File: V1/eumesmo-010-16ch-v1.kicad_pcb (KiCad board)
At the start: 4 copper layers, 128 x 67.8 mm, 284 parts, among them J1 250-208, J2 250-208, J3 250-208, J4 250-208, J5 250-202, J6 USB_C_Receptacle_USB2.0, J7 ETHERNET, Q1 WPM2015-3/TR, Q2 MMUN2211LT3G, Q3 UMH3N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

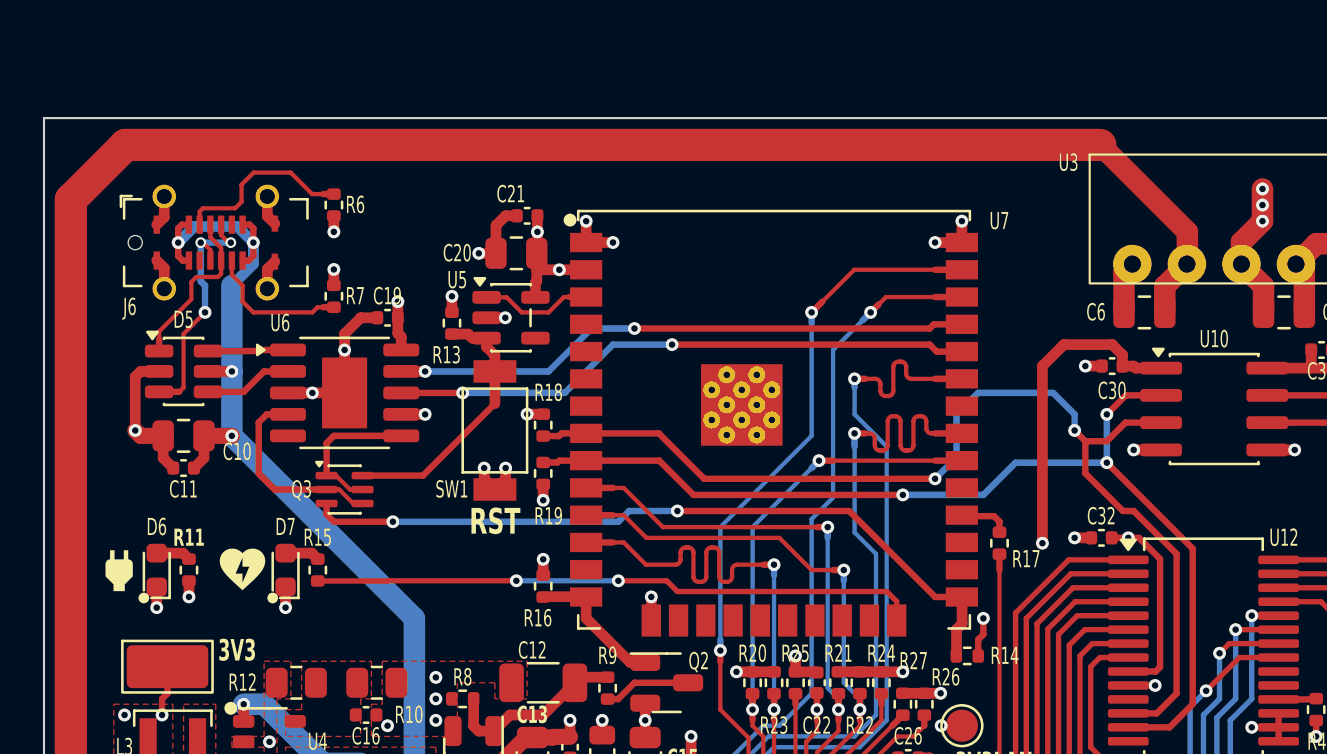
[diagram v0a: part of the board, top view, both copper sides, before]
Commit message: Power and heartbeat leds repositioned.
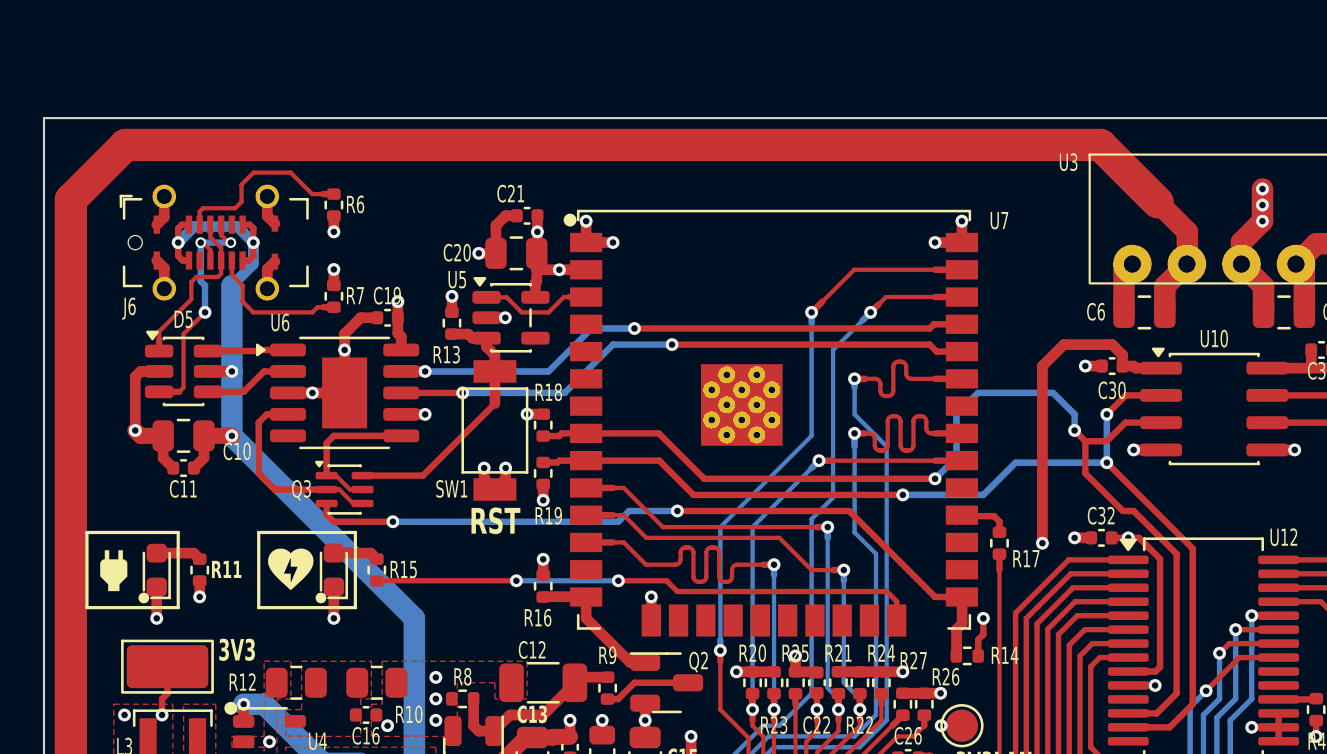
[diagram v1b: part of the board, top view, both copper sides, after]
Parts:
- moved R15 2.75 mm to (105.3, 87.3)
- moved D7 2.25 mm to (103.3, 87.3)
- moved REF** 2.25 mm to (101.3, 87.3)
- moved R11 0.50 mm to (97.0, 87.3)
- moved REF** 0.25 mm to (93.0, 87.3)
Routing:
- net /MCU/CPUOK: track 28.3 -> 25.5 mm
- net GND: track 72.2 -> 73.2 mm
- net /Power/3V3LED: track 1.61 -> 2.11 mm
- net /MCU/CPULED: track 1.61 -> 2.11 mm
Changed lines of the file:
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@@
 	(footprint "Tales:R_0402_1005Metric"
 		(layer "F.Cu")
-		(at 102.52 87.33 90)
+		(at 105.27 87.33 90)
 		(descr "Resistor SMD 0402 (1005 Metric), square (rectangular) end terminal, IPC_7351 nominal, (Body size source: IPC-SM-782 page 72, https://www.pcb-3d.com/wordpress/wp-content/uploads/ipc-sm-782a_amendment_1_and_2.pdf), generated with kicad-footprint-generator")
 		(tags "resistor")
 		(property "Reference" "R15"
-			(at 1.5 0 0)
+			(at 0 1.25 0)
 			(layer "F.SilkS")
 			(effects
@@
 		(tags "LED")
 		(property "Reference" "D6"
-			(at 2 0 180)
+			(at 0 0 180)
 			(layer "F.SilkS")
+			(hide yes)
 			(effects
 				(font
@@
 	(footprint "Tales:Icon_Power_Plug"
 		(layer "F.Cu")
-		(at 93.27 87.33)
+		(at 93.02 87.33)
 		(descr "Power plug from Material Design Icons")
 		(property "Reference" "REF**"
@@
 	(footprint "Tales:LED_0603_1608Metric"
 		(layer "F.Cu")
-		(at 101.02 87.33 90)
+		(at 103.27 87.33 90)
 		(descr "LED SMD 0603 (1608 Metric), square (rectangular) end terminal, IPC_7351 nominal, (Body size source: http://www.tortai-tech.com/upload/download/2011102023233369053.pdf), generated with kicad-footprint-generator")
 		(tags "LED")
 		(property "Reference" "D7"
-			(at 2 0 180)
+			(at 0 0 180)
 			(layer "F.SilkS")
+			(hide yes)
 			(effects
 				(font
@@
 	(footprint "Tales:R_0402_1005Metric"
 		(layer "F.Cu")
-		(at 96.52 87.33 90)
+		(at 97.02 87.33 90)
 		(descr "Resistor SMD 0402 (1005 Metric), square (rectangular) end terminal, IPC_7351 nominal, (Body size source: IPC-SM-782 page 72, https://www.pcb-3d.com/wordpress/wp-content/uploads/ipc-sm-782a_amendment_1_and_2.pdf), generated with kicad-footprint-generator")
 		(tags "resistor")
 		(property "Reference" "R11"
-			(at 1.5 0 0)
+			(at 0 1.25 0)
 			(layer "F.SilkS")
 			(effects
@@
 	(footprint "Tales:Icon_Heart_Flash"
 		(layer "F.Cu")
-		(at 99.02 87.33)
+		(at 101.27 87.33)
 		(descr "Heart with flash from Material Design Icons")
 		(property "Reference" "REF**"
@@
 	)
 	(gr_rect
+		(start 91.77 85.58)
+		(end 96.02 89.08)
+		(stroke
+			(width 0.15)
+			(type solid)
+		)
+		(fill no)
+		(layer "F.SilkS")
+	)
+	(gr_rect
+		(start 99.77 85.58)
+		(end 104.27 89.08)
+		(stroke
+			(width 0.15)
+			(type solid)
+		)
+		(fill no)
+		(layer "F.SilkS")
+	)
+	(gr_rect
 		(start 105.77 132.455)
 		(end 113.27 133.705)
@@
 	)
 	(segment
-		(start 105.77 87.83)
-		(end 105.76 87.84)
-		(width 0.25)
-		(layer "F.Cu")
-		(net "/MCU/CPUOK")
-	)
-	(segment
 		(start 129.485 89.68)
 		(end 129.485 88.795)
@@
 	(segment
 		(start 111.77 87.83)
-		(end 105.77 87.83)
+		(end 105.28 87.83)
 		(width 0.25)
 		(layer "F.Cu")
@@
 	)
 	(segment
-		(start 105.76 87.84)
-		(end 102.52 87.84)
-		(width 0.25)
-		(layer "F.Cu")
-		(net "/MCU/CPUOK")
-	)
-	(segment
 		(start 118.77 87.83)
 		(end 116.52 87.83)
@@
 	)
 	(segment
-		(start 102.2425 86.5425)
-		(end 102.52 86.82)
+		(start 104.9925 86.5425)
+		(end 105.27 86.82)
 		(width 0.5)
 		(layer "F.Cu")
@@
 	)
 	(segment
-		(start 101.02 86.5425)
-		(end 102.2425 86.5425)
+		(start 103.27 86.5425)
+		(end 104.9925 86.5425)
 		(width 0.5)
 		(layer "F.Cu")
@@
 	)
 	(segment
-		(start 138.97 67.53)
-		(end 143.02 71.58)
-		(width 1)
+		(start 91.02 70.08)
+		(end 91.02 104.33)
+		(width 1.5)
 		(layer "F.Cu")
 		(net "+24V")
@@
 	)
 	(segment
-		(start 141.97 75.33)
-		(end 141.97 74.11)
-		(width 1)
+		(start 94.22 107.53)
+		(end 94.22 109.58)
+		(width 1.5)
 		(layer "F.Cu")
 		(net "+24V")
 	)
 	(segment
-		(start 94.22 107.53)
-		(end 94.22 109.58)
+		(start 93.57 67.53)
+		(end 91.02 70.08)
 		(width 1.5)
 		(layer "F.Cu")
@@
 	)
 	(segment
-		(start 91.02 104.33)
-		(end 94.22 107.53)
+		(start 141.645 70.205)
+		(end 138.97 67.53)
 		(width 1.5)
 		(layer "F.Cu")
@@
 	)
 	(segment
-		(start 93.57 67.53)
-		(end 91.02 70.08)
+		(start 141.97 75.33)
+		(end 141.97 74.11)
+		(width 1)
+		(layer "F.Cu")
+		(net "+24V")
+	)
+	(segment
+		(start 91.02 104.33)
+		(end 94.22 107.53)
 		(width 1.5)
 		(layer "F.Cu")
@@
 	)
 	(segment
-		(start 143.02 71.58)
-		(end 143.02 73.06)
+		(start 141.645 70.205)
+		(end 143.02 71.58)
 		(width 1)
 		(layer "F.Cu")
@@
 	)
 	(segment
-		(start 91.02 70.08)
-		(end 91.02 104.33)
-		(width 1.5)
+		(start 143.02 71.58)
+		(end 143.02 73.06)
+		(width 1)
 		(layer "F.Cu")
 		(net "+24V")
@@
 	)
 	(segment
-		(start 95.02 88.1175)
-		(end 95.02 89.08)
-		(width 0.5)
-		(layer "F.Cu")
-		(net "GND")
-	)
-	(segment
 		(start 114.27 129.33)
 		(end 113.795 129.33)
@@
 	)
 	(segment
-		(start 101.02 88.1175)
-		(end 101.02 89.08)
-		(width 0.5)
-		(layer "F.Cu")
-		(net "GND")
-	)
-	(segment
 		(start 131.53 93.07)
 		(end 130.77 93.07)
@@
 	)
 	(segment
+		(start 103.27 88.1175)
+		(end 103.27 89.58)
+		(width 0.5)
+		(layer "F.Cu")
+		(net "GND")
+	)
+	(segment
 		(start 123.27 100.83)
 		(end 123.92 100.18)
@@
 	)
 	(segment
+		(start 95.02 88.1175)
+		(end 95.02 89.58)
+		(width 0.5)
+		(layer "F.Cu")
+		(net "GND")
+	)
+	(segment
 		(start 111.52 97.03)
 		(end 112.52 97.03)
@@
 	)
 	(via
-		(at 101.02 89.08)
+		(at 103.27 89.58)
 		(size 0.6)
 		(drill 0.3)
@@
 	)
 	(via
-		(at 95.02 89.08)
+		(at 95.02 89.58)
 		(size 0.6)
 		(drill 0.3)
@@
 	)
 	(segment
-		(start 96.52 87.84)
-		(end 96.52 88.58)
+		(start 97.02 87.84)
+		(end 97.02 88.58)
 		(width 0.5)
 		(layer "F.Cu")
@@
 	)
 	(via
-		(at 96.52 88.58)
+		(at 97.02 88.58)
 		(size 0.6)
 		(drill 0.3)
@@
 	)
 	(segment
-		(start 96.2425 86.5425)
-		(end 96.52 86.82)
+		(start 96.7425 86.5425)
+		(end 97.02 86.82)
 		(width 0.5)
 		(layer "F.Cu")
@@
 	(segment
 		(start 95.02 86.5425)
-		(end 96.2425 86.5425)
+		(end 96.7425 86.5425)
 		(width 0.5)
 		(layer "F.Cu")
